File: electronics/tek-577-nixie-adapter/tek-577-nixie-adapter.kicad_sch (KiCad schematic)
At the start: 4 parts, among them J1 C, J2 B, J3 E, J4 Conn_01x10_Socket

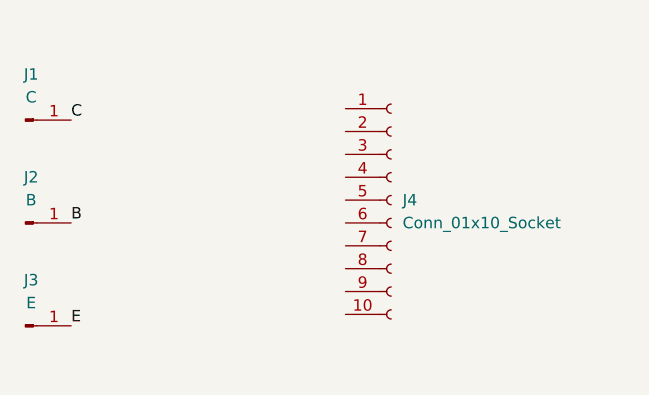
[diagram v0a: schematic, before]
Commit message: adding symbols
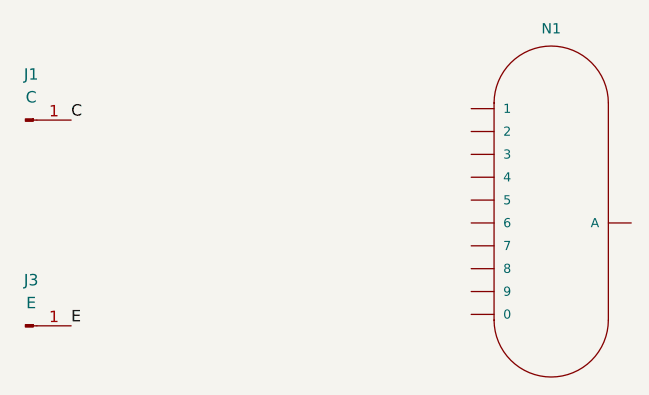
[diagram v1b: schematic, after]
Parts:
- removed J2: B, MountingHole:MountingHole_4mm_Pad_TopBottom, symbol Connector:Conn_01x01_Pin
- removed J4: Conn_01x10_Socket, symbol Connector:Conn_01x10_Socket
- added N1: IN-4, nixies-us_IN-4-DSUB, symbol nixies-us:IN-4
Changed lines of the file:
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@@
     (effects (font (size 1.27 1.27)) (justify left bottom))
   )
-  (label "B" (at 81.28 83.82 0) (fields_autoplaced)
-    (effects (font (size 1.27 1.27)) (justify left bottom))
-  )
-  (symbol (lib_id "Connector:Conn_01x01_Pin") (at 76.2 83.82 0) (unit 1)
+  (symbol (lib_id "nixies-us:IN-4") (at 135.89 83.82 0) (unit 1)
     (in_bom yes) (on_board yes) (dnp no) (fields_autoplaced)
-    (property "Reference" "J2" (at 76.835 78.74 0)
-      (effects (font (size 1.27 1.27)))
+    (property "Reference" "N1" (at 134.62 62.23 0)
+      (effects (font (size 1.143 1.143)))
     )
-    (property "Value" "B" (at 76.835 81.28 0)
-      (effects (font (size 1.27 1.27)))
+    (property "Value" "IN-4" (at 135.89 83.82 0)
+      (effects (font (size 1.143 1.143)) (justify left bottom) hide)
     )
-    (property "Footprint" "MountingHole:MountingHole_4mm_Pad_TopBottom" (at 76.2 83.82 0)
+    (property "Footprint" "nixies-us_IN-4-DSUB" (at 136.652 80.01 0)
+      (effects (font (size 0.508 0.508)) hide)
+    )
+    (property "Datasheet" "" (at 135.89 83.82 0)
       (effects (font (size 1.27 1.27)) hide)
     )
-    (property "Datasheet" "~" (at 76.2 83.82 0)
-      (effects (font (size 1.27 1.27)) hide)
-    )
+    (pin "0")
     (pin "1")
-    (instances
-      (project "tek-577-nixie-adapter"
-        (path "/0ef3df54-7667-4802-a3e0-859bd82101b0"
-          (reference "J2") (unit 1)
-        )
-      )
-      (project "tek-577-fixture-proto"
-        (path "/81061b7e-5ca3-40cf-b674-442e1b899f43"
-          (reference "J2") (unit 1)
-        )
-      )
-    )
-  )
-  (symbol (lib_id "Connector:Conn_01x10_Socket") (at 116.84 81.28 0) (unit 1)
-    (in_bom yes) (on_board yes) (dnp no) (fields_autoplaced)
-    (property "Reference" "J4" (at 118.11 81.28 0)
-      (effects (font (size 1.27 1.27)) (justify left))
-    )
-    (property "Value" "Conn_01x10_Socket" (at 118.11 83.82 0)
-      (effects (font (size 1.27 1.27)) (justify left))
-    )
-    (property "Footprint" "" (at 116.84 81.28 0)
-      (effects (font (size 1.27 1.27)) hide)
-    )
-    (property "Datasheet" "~" (at 116.84 81.28 0)
-      (effects (font (size 1.27 1.27)) hide)
-    )
-    (pin "1")
-    (pin "10")
     (pin "2")
     (pin "3")
@@
     (pin "8")
     (pin "9")
+    (pin "A3")
     (instances
       (project "tek-577-nixie-adapter"
         (path "/0ef3df54-7667-4802-a3e0-859bd82101b0"
-          (reference "J4") (unit 1)
+          (reference "N1") (unit 1)
         )
       )

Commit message: working footprints
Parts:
- N1: footprint nixies-us_IN-4-DSUB -> nixie-us:IN-4-DSUB
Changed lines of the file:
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@@
       (effects (font (size 1.143 1.143)) (justify left bottom) hide)
     )
-    (property "Footprint" "nixies-us_IN-4-DSUB" (at 136.652 80.01 0)
+    (property "Footprint" "nixie-us:IN-4-DSUB" (at 136.652 80.01 0)
       (effects (font (size 0.508 0.508)) hide)
     )

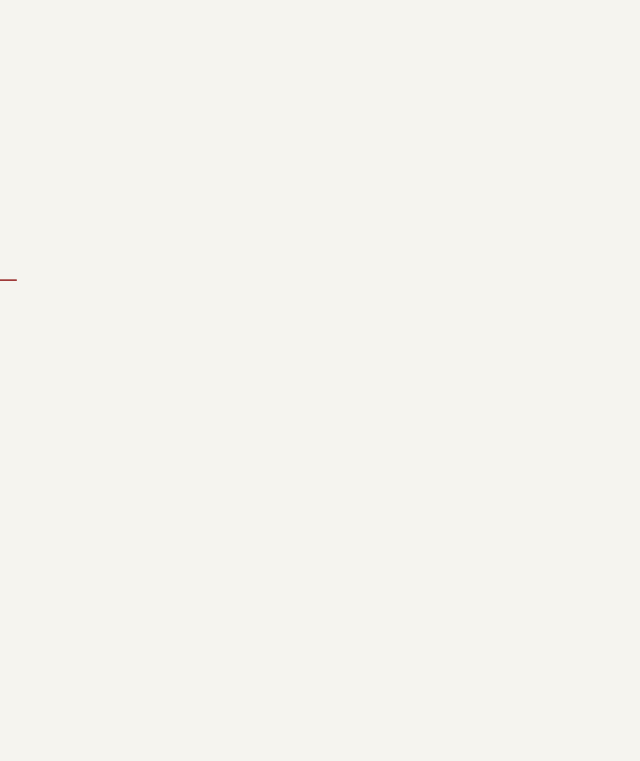
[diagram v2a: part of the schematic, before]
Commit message: adding other tubes
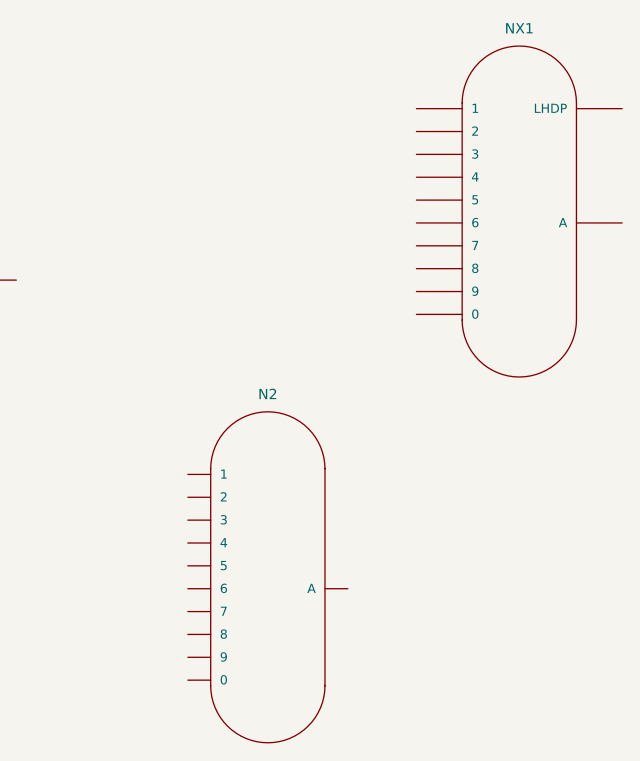
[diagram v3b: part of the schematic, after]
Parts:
- added N2: IN-2, nixies-us_IN-2-DSUB, symbol nixies-us:IN-2
- added NX1: IN-12BIN-12-DSUB, nixies-us_IN-12-DSUB, symbol nixies-us:IN-12BIN-12-DSUB
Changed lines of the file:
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@@
     (effects (font (size 1.27 1.27)) (justify left bottom))
+  )
+  (symbol (lib_id "nixies-us:IN-12BIN-12-DSUB") (at 200.66 77.47 0) (unit 1)
+    (in_bom yes) (on_board yes) (dnp no) (fields_autoplaced)
+    (property "Reference" "NX1" (at 199.39 55.88 0)
+      (effects (font (size 1.143 1.143)))
+    )
+    (property "Value" "IN-12BIN-12-DSUB" (at 200.66 77.47 0)
+      (effects (font (size 1.143 1.143)) (justify left bottom) hide)
+    )
+    (property "Footprint" "nixies-us_IN-12-DSUB" (at 201.422 73.66 0)
+      (effects (font (size 0.508 0.508)) hide)
+    )
+    (property "Datasheet" "" (at 200.66 77.47 0)
+      (effects (font (size 1.27 1.27)) hide)
+    )
+    (pin "0")
+    (pin "1")
+    (pin "2")
+    (pin "3")
+    (pin "4")
+    (pin "5")
+    (pin "6")
+    (pin "7")
+    (pin "8")
+    (pin "9")
+    (pin "A")
+    (pin "LHDP")
+    (instances
+      (project "tek-577-nixie-adapter"
+        (path "/0ef3df54-7667-4802-a3e0-859bd82101b0"
+          (reference "NX1") (unit 1)
+        )
+      )
+    )
+  )
+  (symbol (lib_id "nixies-us:IN-2") (at 172.72 118.11 0) (unit 1)
+    (in_bom yes) (on_board yes) (dnp no) (fields_autoplaced)
+    (property "Reference" "N2" (at 171.45 96.52 0)
+      (effects (font (size 1.143 1.143)))
+    )
+    (property "Value" "IN-2" (at 172.72 118.11 0)
+      (effects (font (size 1.143 1.143)) (justify left bottom) hide)
+    )
+    (property "Footprint" "nixies-us_IN-2-DSUB" (at 173.482 114.3 0)
+      (effects (font (size 0.508 0.508)) hide)
+    )
+    (property "Datasheet" "" (at 172.72 118.11 0)
+      (effects (font (size 1.27 1.27)) hide)
+    )
+    (pin "0")
+    (pin "1")
+    (pin "2")
+    (pin "3")
+    (pin "4")
+    (pin "5")
+    (pin "6")
+    (pin "7")
+    (pin "8")
+    (pin "9")
+    (pin "A")
+    (instances
+      (project "tek-577-nixie-adapter"
+        (path "/0ef3df54-7667-4802-a3e0-859bd82101b0"
+          (reference "N2") (unit 1)
+        )
+      )
+    )
   )
   (symbol (lib_id "nixies-us:IN-4") (at 135.89 83.82 0) (unit 1)

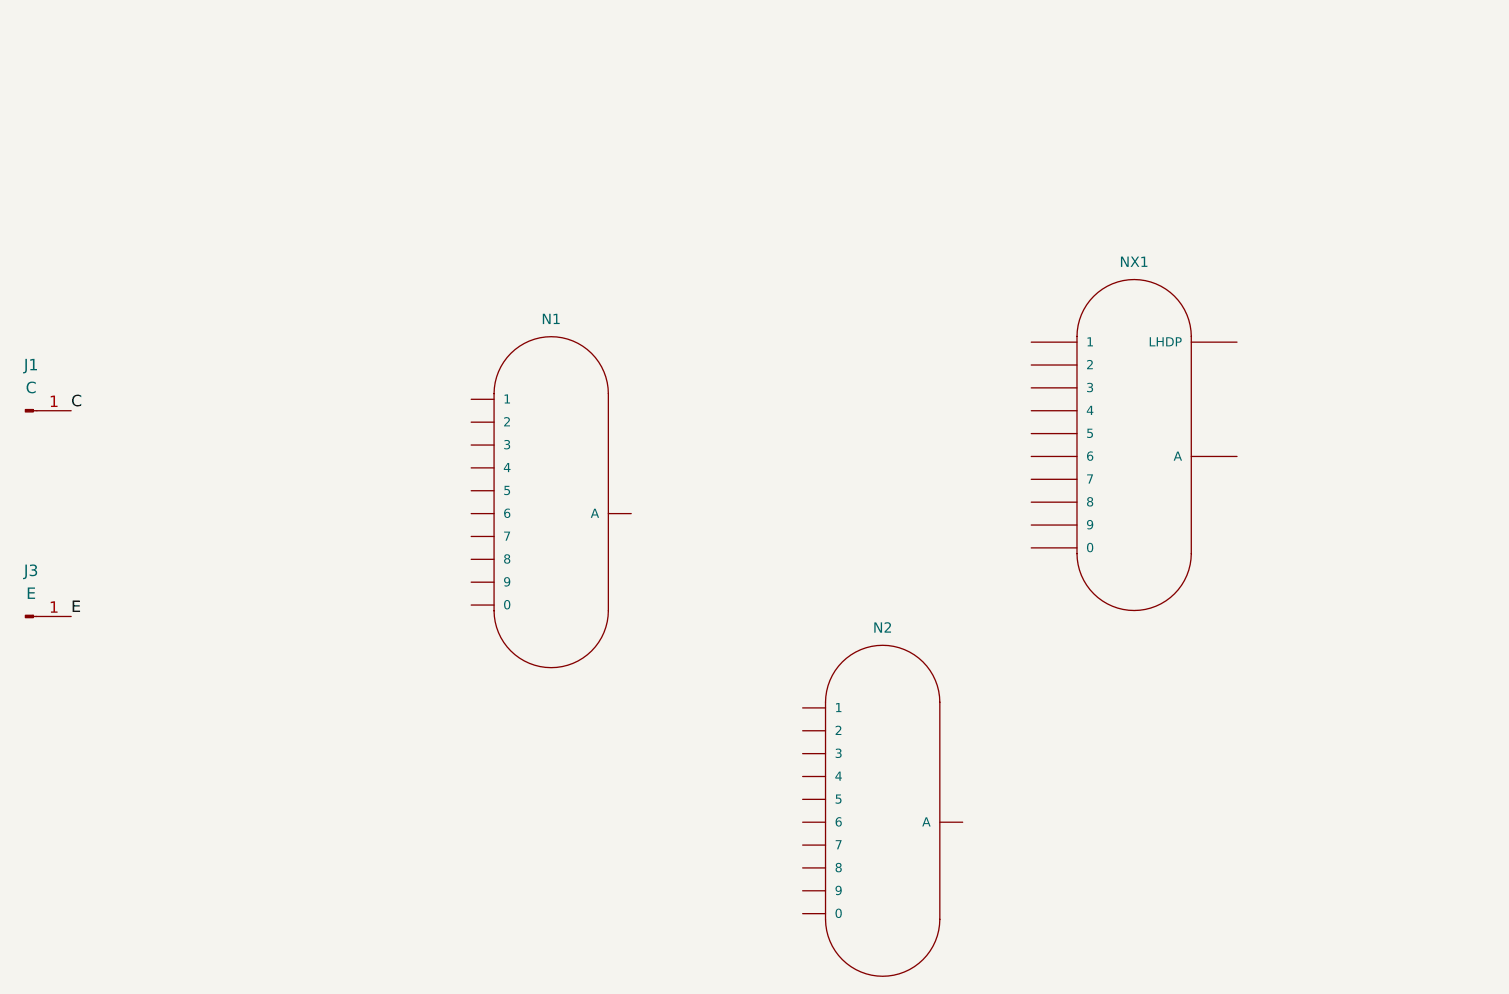
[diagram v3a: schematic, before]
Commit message: adding switch and schematic done
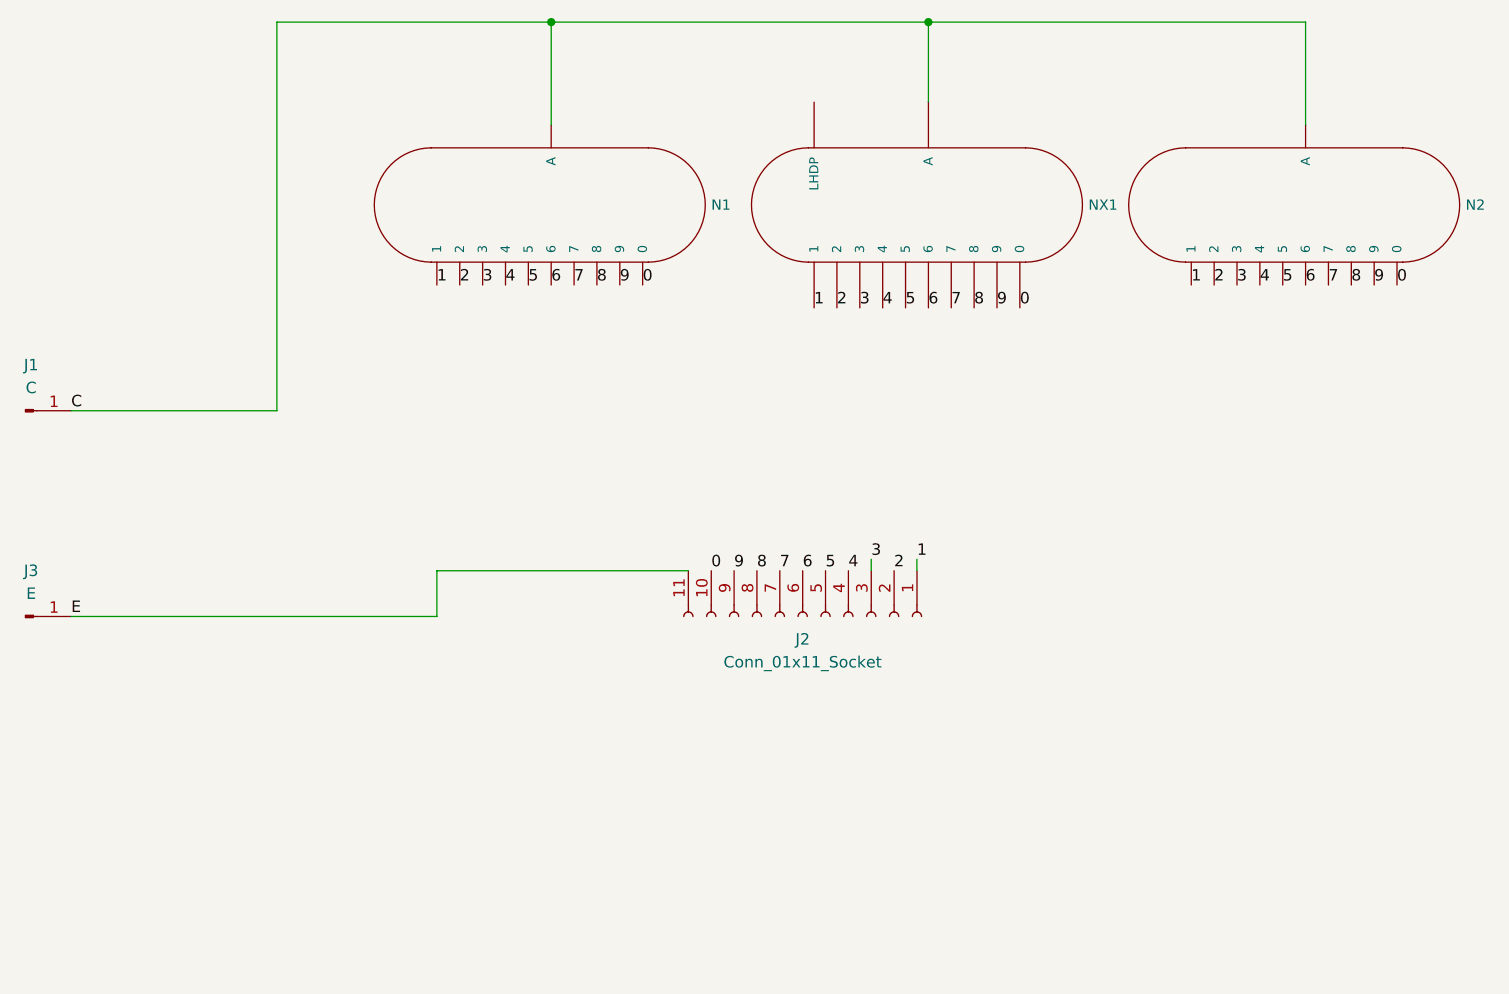
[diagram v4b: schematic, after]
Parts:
- added J2: Conn_01x11_Socket, symbol Connector:Conn_01x11_Socket
- N2: footprint nixies-us_IN-2-DSUB -> (none)
- NX1: footprint nixies-us_IN-12-DSUB -> (none)
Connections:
- net C: now also N1.A3 (A), N2.A, NX1.A
- net E: now also J2.11 (Pin_11)
- net 0: now reaches NX1.0
- net 0: now also N1.0, N2.0, J2.10 (Pin_10)
- net 1: now reaches NX1.1
- net 1: now also N1.1, N2.1, J2.1 (Pin_1)
- net 2: now reaches NX1.2
- net 2: now also N1.2, N2.2, J2.2 (Pin_2)
- net 3: now reaches NX1.3
- net 3: now also N1.3, N2.3, J2.3 (Pin_3)
- net 4: now reaches NX1.4
- net 4: now also N1.4, N2.4, J2.4 (Pin_4)
- net 5: now reaches NX1.5
- net 5: now also N1.5, N2.5, J2.5 (Pin_5)
- net 6: now reaches NX1.6
- net 6: now also N1.6, N2.6, J2.6 (Pin_6)
- net 7: now reaches NX1.7
- net 7: now also N1.7, N2.7, J2.7 (Pin_7)
- net 8: now reaches NX1.8
- net 8: now also N1.8, N2.8, J2.8 (Pin_8)
- net 9: now reaches NX1.9
- net 9: now also N1.9, N2.9, J2.9 (Pin_9)
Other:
- moved on the sheet: N1, N2, NX1

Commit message: adding the footprints, which only loaded on mac for some reason
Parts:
- J2: footprint (none) -> Grayhill-Switch:Grayhill Single Pole 10 Position Switch
- N2: footprint (none) -> nixie-us:IN-2-DSUB
- NX1: footprint (none) -> nixie-us:IN-12-DSUB
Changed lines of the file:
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@@
       (effects (font (size 1.143 1.143)) (justify left bottom) hide)
     )
-    (property "Footprint" "" (at 172.72 47.498 0)
+    (property "Footprint" "nixie-us:IN-12-DSUB" (at 172.72 47.498 0)
       (effects (font (size 0.508 0.508)) hide)
     )
@@
       (effects (font (size 1.27 1.27)))
     )
-    (property "Footprint" "" (at 162.56 95.25 0)
+    (property "Footprint" "Grayhill-Switch:Grayhill Single Pole 10 Position Switch" (at 162.56 95.25 0)
       (effects (font (size 1.27 1.27)) hide)
     )
@@
       (effects (font (size 1.143 1.143)) (justify left bottom) hide)
     )
-    (property "Footprint" "" (at 214.63 47.498 0)
+    (property "Footprint" "nixie-us:IN-2-DSUB" (at 214.63 47.498 0)
       (effects (font (size 0.508 0.508)) hide)
     )

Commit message: board design done
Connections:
- net E: now also NX1.LHDP
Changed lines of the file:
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@@
+    (effects (font (size 1.27 1.27)) (justify left bottom))
+  )
+  (label "E" (at 163.83 38.1 0) (fields_autoplaced)
     (effects (font (size 1.27 1.27)) (justify left bottom))
   )

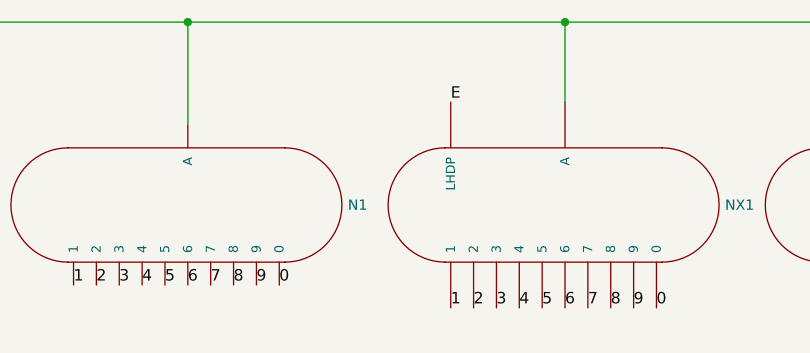
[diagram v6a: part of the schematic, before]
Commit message: fixing decimal point short with jumper
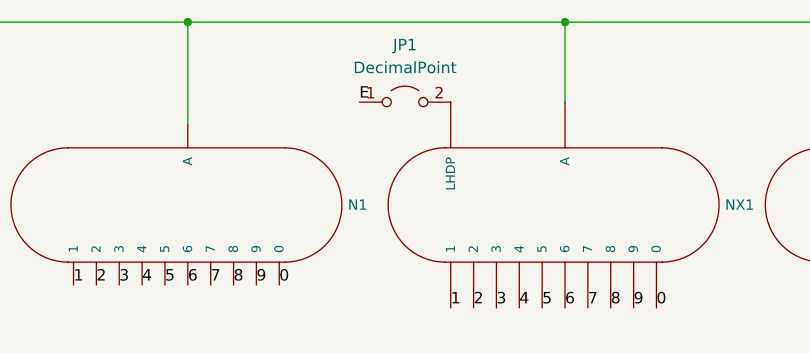
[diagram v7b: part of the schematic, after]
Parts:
- added JP1: DecimalPoint, TestPoint:TestPoint_2Pads_Pitch2.54mm_Drill0.8mm, symbol Jumper:Jumper_2_Open
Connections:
- net E: now also JP1.1 (A); no longer NX1.LHDP
- new net: JP1.2 (B), NX1.LHDP
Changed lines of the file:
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@@
     (effects (font (size 1.27 1.27)) (justify left bottom))
   )
-  (label "E" (at 163.83 38.1 0) (fields_autoplaced)
+  (label "E" (at 153.67 38.1 0) (fields_autoplaced)
     (effects (font (size 1.27 1.27)) (justify left bottom))
   )
@@
         )
       )
+    )
+  )
+  (symbol (lib_id "Jumper:Jumper_2_Open") (at 158.75 38.1 0) (unit 1)
+    (in_bom yes) (on_board yes) (dnp no) (fields_autoplaced)
+    (property "Reference" "JP1" (at 158.75 31.75 0)
+      (effects (font (size 1.27 1.27)))
+    )
+    (property "Value" "DecimalPoint" (at 158.75 34.29 0)
+      (effects (font (size 1.27 1.27)))
+    )
+    (property "Footprint" "TestPoint:TestPoint_2Pads_Pitch2.54mm_Drill0.8mm" (at 158.75 38.1 0)
+      (effects (font (size 1.27 1.27)) hide)
+    )
+    (property "Datasheet" "~" (at 158.75 38.1 0)
+      (effects (font (size 1.27 1.27)) hide)
+    )
+    (pin "1")
+    (pin "2")
+    (instances
+      (project "tek-577-nixie-adapter"
+        (path "/0ef3df54-7667-4802-a3e0-859bd82101b0"
+          (reference "JP1") (unit 1)
+        )
+      )
